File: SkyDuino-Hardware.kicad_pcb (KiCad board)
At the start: 4 copper layers, 123 x 56 mm, 80 parts, among them J1 24V, J11 DBG, J12 USB-A RMT, J13 DISP, J14 USB_C Artisan, J2 BT, J4 Drum, J5 Exhaust, J6 Cooling, J7 Cooling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

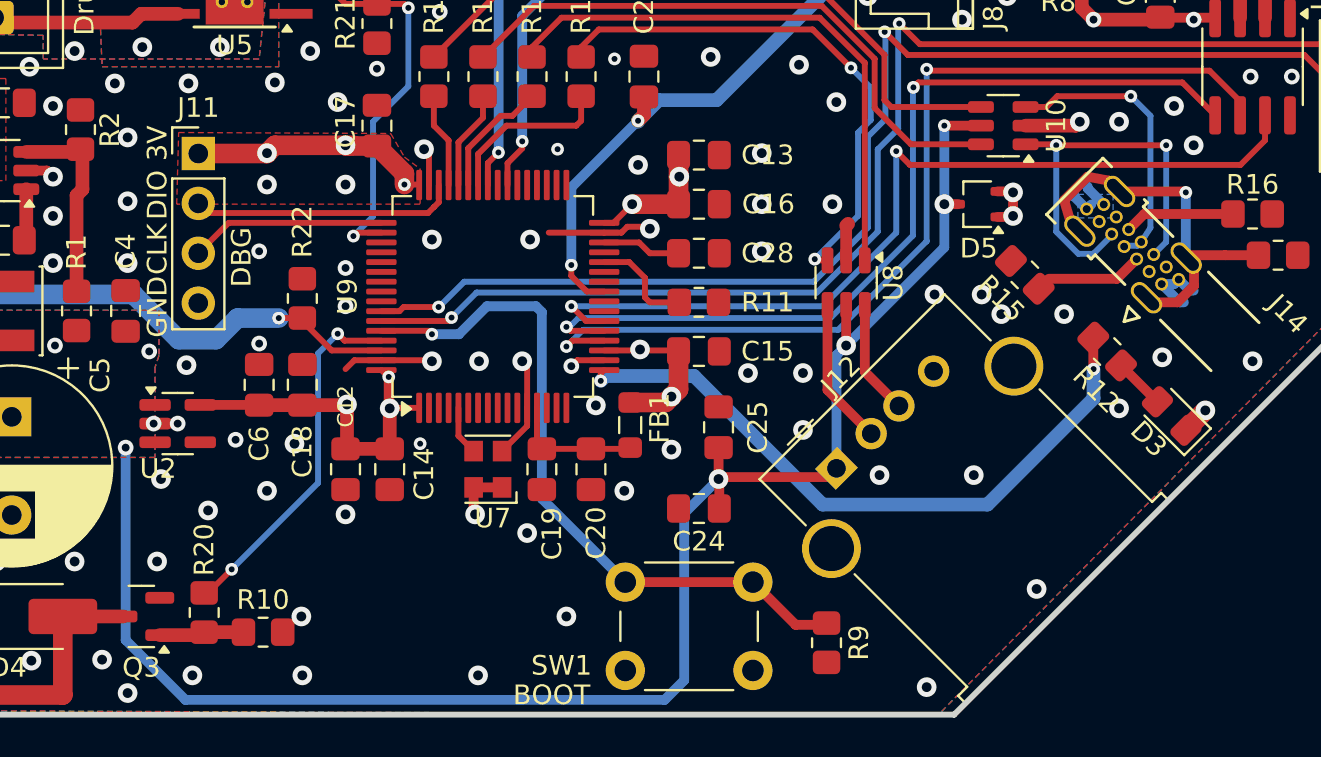
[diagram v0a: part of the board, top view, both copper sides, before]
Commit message: Increase 5v track width
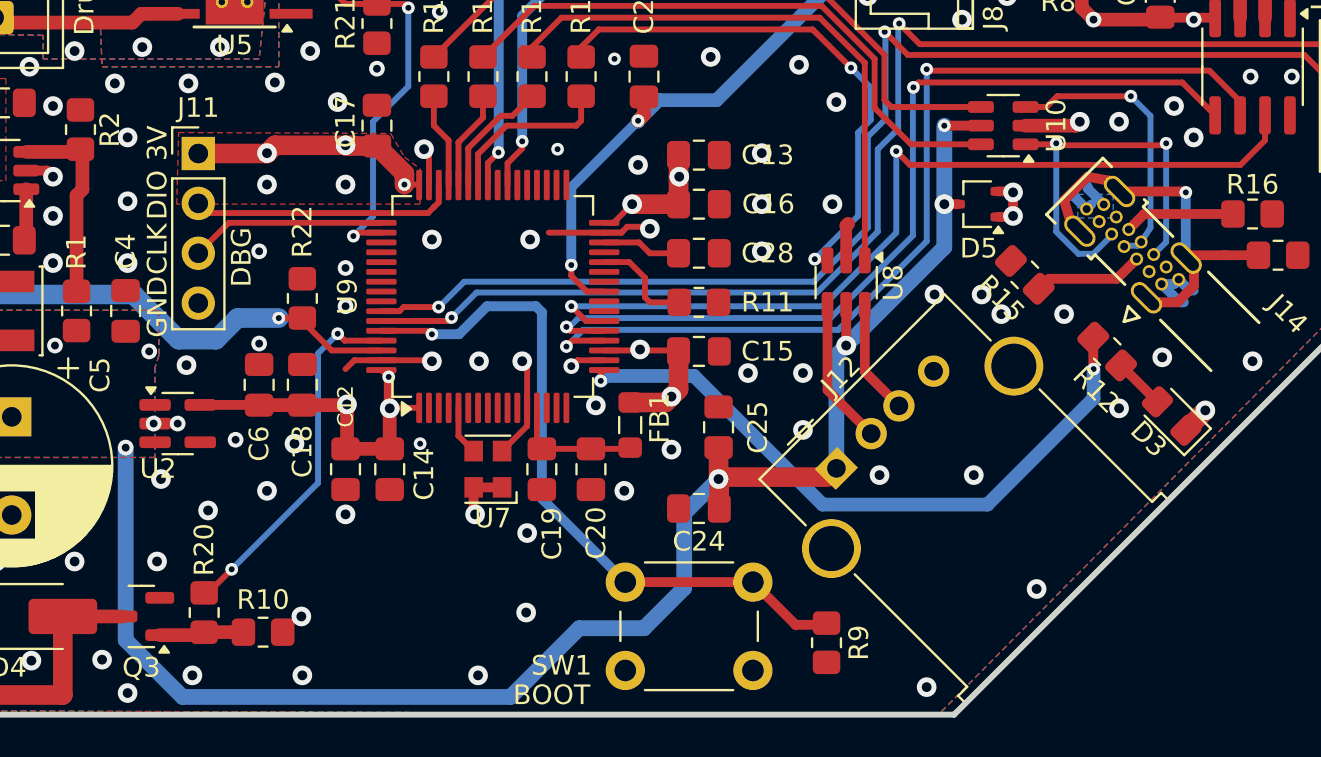
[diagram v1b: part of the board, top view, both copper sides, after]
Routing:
- net +5V: track 106.8 -> 104.3 mm
